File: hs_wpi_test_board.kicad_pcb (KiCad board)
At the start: 2 copper layers, 74.9 x 44.4 mm, 34 parts, among them J1 Raspberry_Pi_2_3, Q1 Q_NPN_EBC, Q10 Q_NPN_EBC, Q2 Q_NPN_EBC, Q3 Q_NPN_EBC, Q4 Q_NPN_EBC, Q5 Q_NPN_EBC, Q6 Q_NPN_EBC, Q7 Q_NPN_EBC, Q8 Q_NPN_EBC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

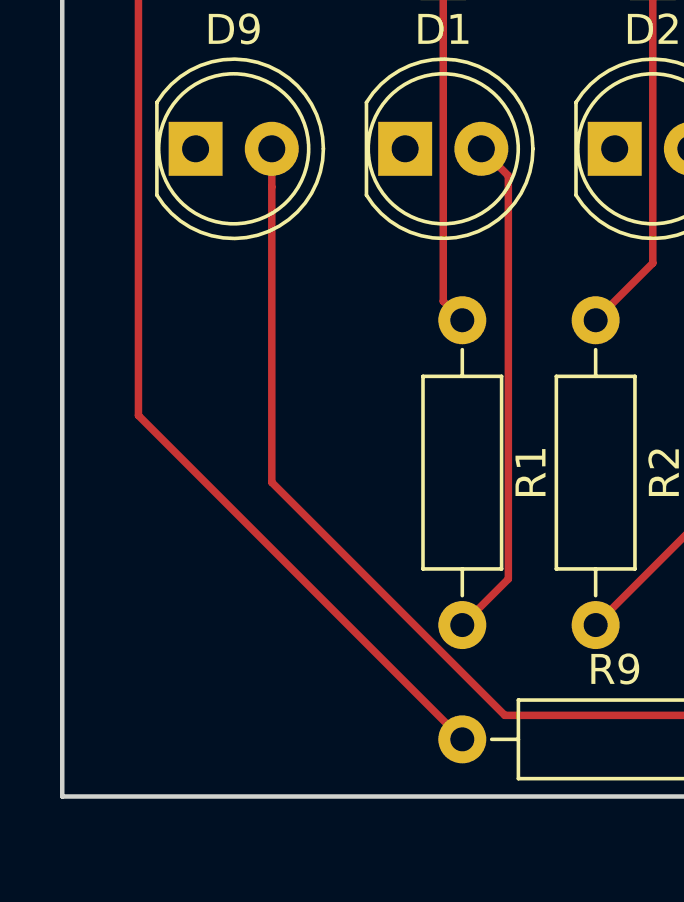
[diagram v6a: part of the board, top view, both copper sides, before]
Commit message: silkscreen text
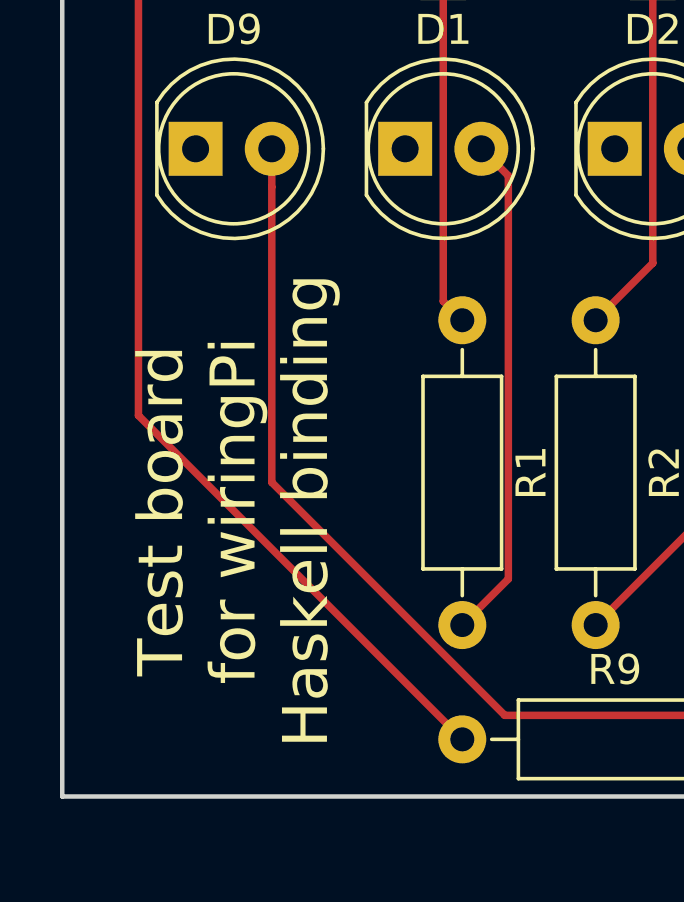
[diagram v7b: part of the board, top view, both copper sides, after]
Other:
- board text added: "Test board for wiringPi Haskell binding"
- board text added: "https://hackage.haskell.org/package/wiringPi Patrick Pelletier 2017-08-07"
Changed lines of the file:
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@@
     (area 0 0 0 0)
     (thickness 1.6)
-    (drawings 8)
+    (drawings 10)
     (tracks 247)
     (zones 0)
@@
     )
   )
+  (gr_text "Test board\nfor wiringPi\nHaskell binding" (at 102.235 109.855 90) (layer F.SilkS)
+    (effects (font (size 1.5 1.5) (thickness 0.3)))
+  )
+  (gr_text "https://hackage.haskell.org/package/wiringPi   Patrick Pelletier 2017-08-07" (at 133.35 94.615) (layer B.SilkS)
+    (effects (font (size 1 1) (thickness 0.25)) (justify mirror))
+  )
   (gr_line (start 96.52 119.38) (end 96.52 74.93) (angle 90) (layer Edge.Cuts) (width 0.15))
